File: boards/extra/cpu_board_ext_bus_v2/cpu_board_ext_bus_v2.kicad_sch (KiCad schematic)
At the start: 24 parts, among them J1 Exp. Conn. A, J2 Exp. Conn. B, J3 Power, J4 Exp. Conn. C

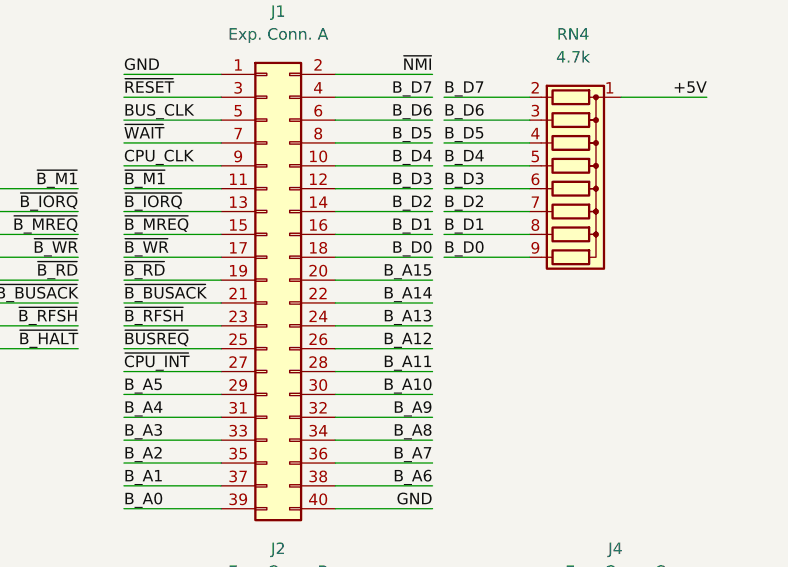
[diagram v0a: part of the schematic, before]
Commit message: Removed CPU connection A14 and A15 from Expansion Bus Connector B.
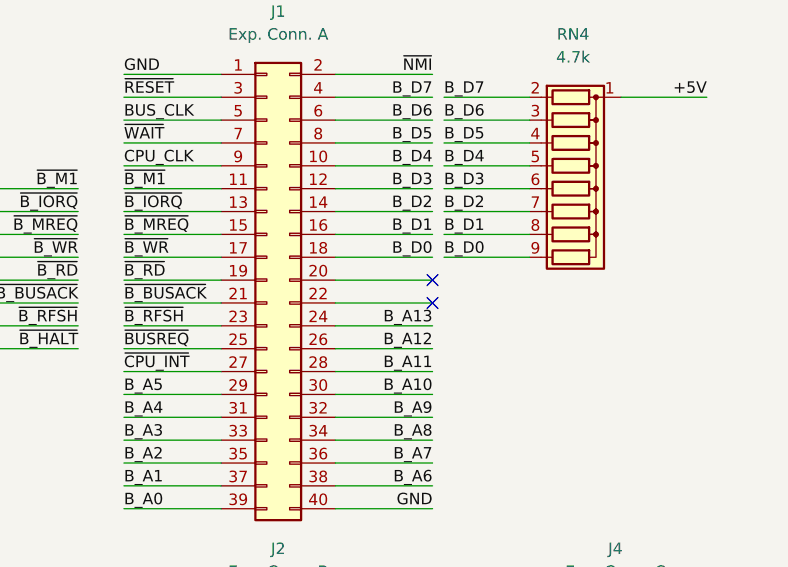
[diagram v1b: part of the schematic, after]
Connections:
- net B_A14: no longer J1.22 (Pin_22)
- net B_A15: no longer J1.20 (Pin_20)
- no-connect marks 27 -> 29
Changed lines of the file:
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@@
   (title_block
     (title "SZC-1 board with Expansion Bus C V2")
-    (date "2024-01-23")
+    (date "2024-03-15")
     (rev "2.0")
   )
@@
   (no_connect (at 356.235 110.49))
   (no_connect (at 356.235 107.95))
+  (no_connect (at 356.235 64.135))
   (no_connect (at 325.12 153.67))
   (no_connect (at 356.235 113.03))
@@
   (no_connect (at 353.06 153.67))
   (no_connect (at 356.235 138.43))
+  (no_connect (at 356.235 66.675))
   (no_connect (at 356.235 120.65))
   (no_connect (at 356.235 130.81))
@@
     (effects (font (size 1.27 1.27)) (justify right bottom))
   )
-  (label "B_A14" (at 356.235 66.675 180) (fields_autoplaced)
-    (effects (font (size 1.27 1.27)) (justify right bottom))
-  )
   (label "USER12" (at 356.235 107.95 180) (fields_autoplaced)
     (effects (font (size 1.27 1.27)) (justify right bottom))
@@
     (effects (font (size 1.27 1.27)) (justify left bottom))
   )
-  (label "B_A15" (at 356.235 64.135 180) (fields_autoplaced)
-    (effects (font (size 1.27 1.27)) (justify right bottom))
-  )
   (label "GND" (at 325.12 161.29 0) (fields_autoplaced)

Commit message: Preparation for ordering with PCBWay.
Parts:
- C1, C2: MPN (none) -> FG28X7R1H104KNT06; Manufacturer (none) -> TDK; Package (none) -> Plugin,P=5mm
- CP1: MPN (none) -> ECA1HM100I; Manufacturer (none) -> PANASONIC; Package (none) -> Plugin,D5xL11mm
- CP2: MPN (none) -> KS104M050C07RR0VH2FP0; Manufacturer (none) -> CX(Dongguan Chengxing Elec); Package (none) -> Plugin,D4xL7mm
- D1: MPN (none) -> HLMP-1700; Manufacturer (none) -> Broadcom/AVAGO; Package (none) -> LED_D3.0mm
- J1: MPN (none) -> X9555WR-2x20-6TV01; Manufacturer (none) -> XKB Connectivity; Package (none) -> Push-Pull,P=2.54mm
- J2: MPN (none) -> X9555WR-2x17-6TV01; Manufacturer (none) -> XKB Connectivity; Package (none) -> Push-Pull,P=2.54mm
- J3: MPN (none) -> X9555WR-2x10-6TV01; Manufacturer (none) -> XKB Connectivity; Package (none) -> Push-Pull,P=2.54mm
- J4: MPN (none) -> 75867-132LF; Manufacturer (none) -> Amphenol ICC; Package (none) -> Plugin
- R3: MPN (none) -> MFR2WSFTE73-1K; Manufacturer (none) -> YAGEO; Package (none) -> Plugin
- RN2, RN3, RN4: MPN (none) -> A09-472JP; Manufacturer (none) -> FH (Guangdong Fenghua Advanced Tech); Package (none) -> SIP-9-2.54mm

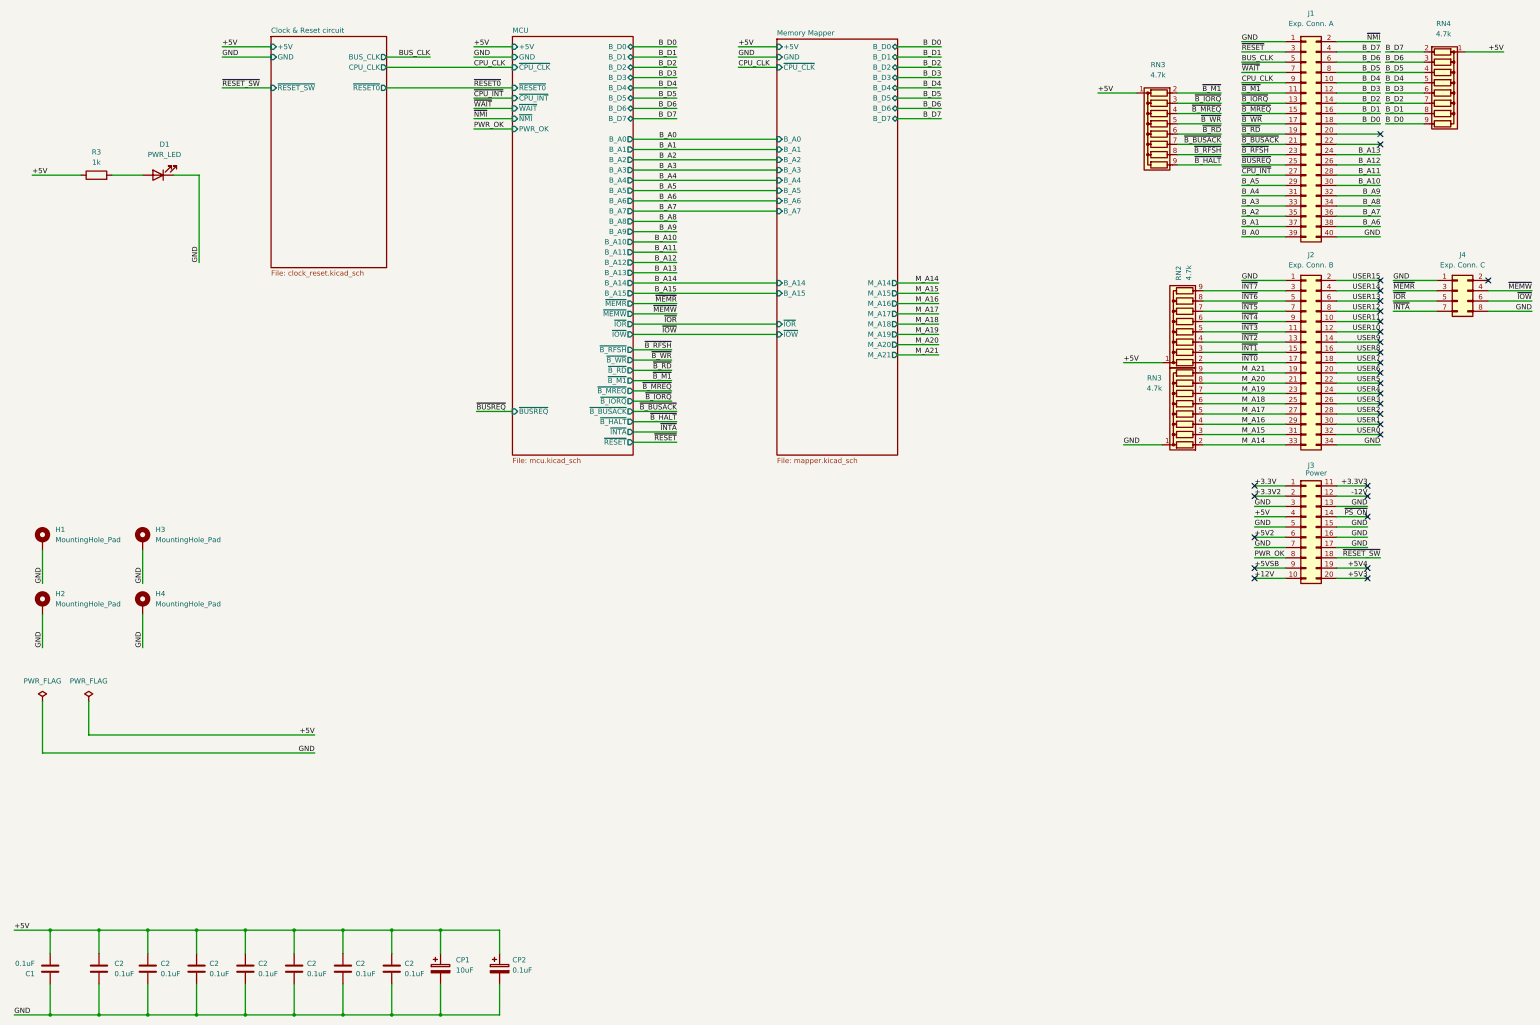
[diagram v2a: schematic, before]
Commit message: Upgraded board to KiCad 8 and imported design rules from the PCBWay website.
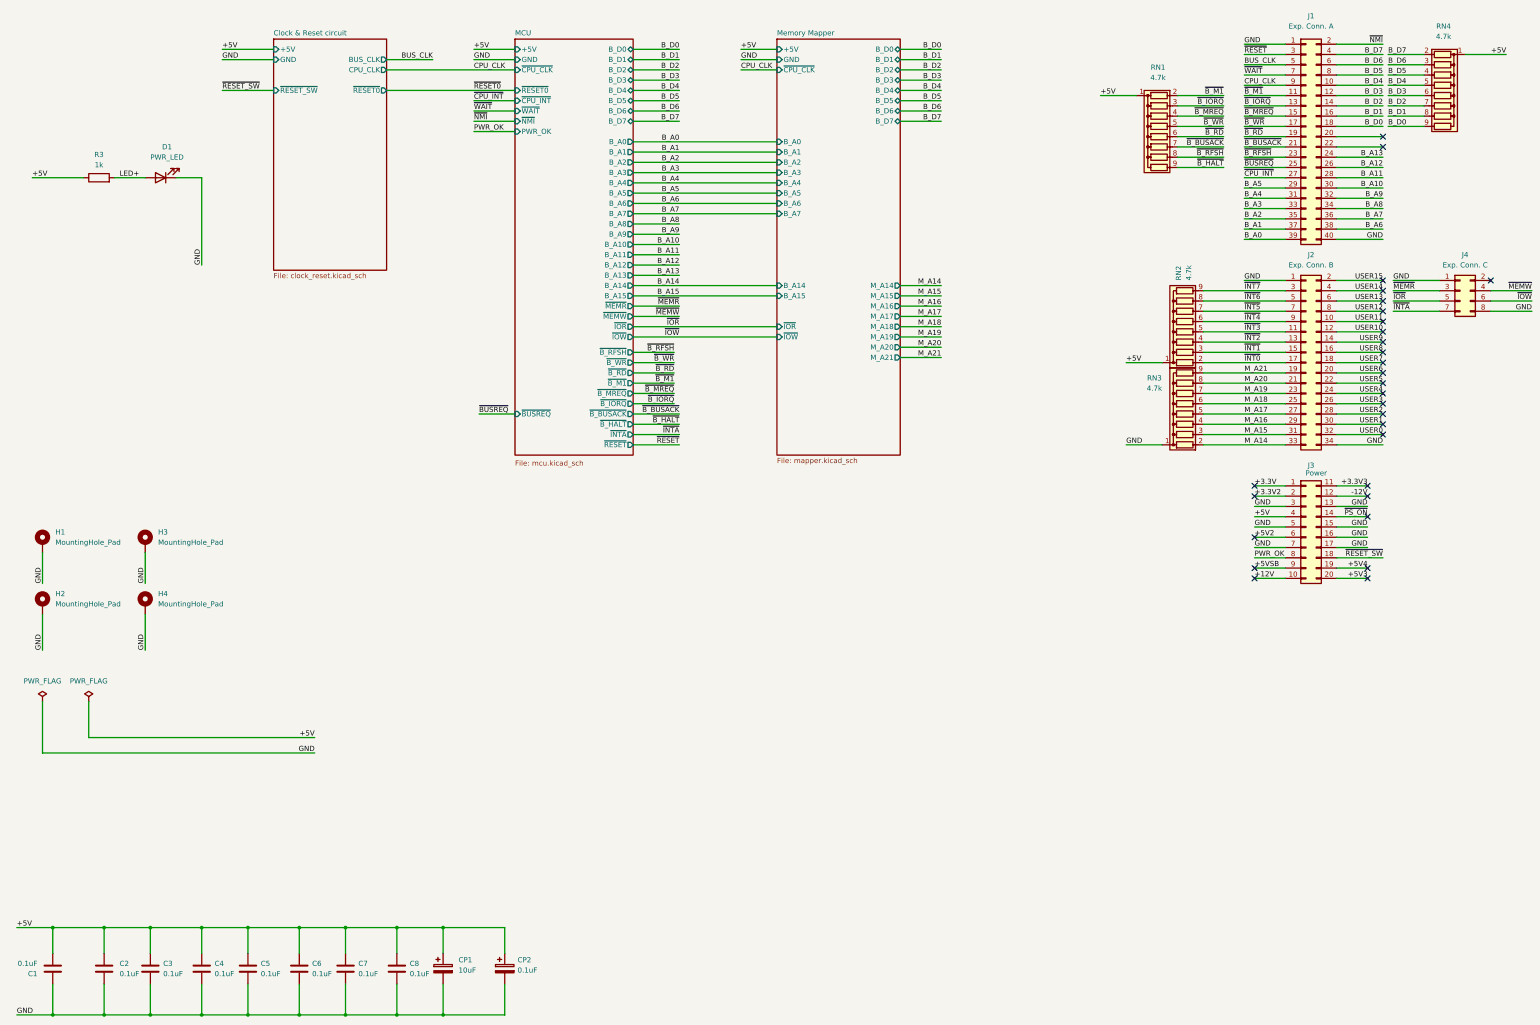
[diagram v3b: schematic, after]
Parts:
- removed C2 (x7): 0.1uF, Capacitor_THT:C_Disc_D5.0mm_W2.5mm_P2.50mm, symbol Device:C
- added C2, C3, C4, C5, C6, C7, C8: 0.1uF, Capacitor_THT:C_Disc_D5.0mm_W2.5mm_P2.50mm, symbol Device:C
- renumbered RN3 to RN1
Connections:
- net +5V: now also C2.1, C3.1, C4.1, C5.1, C6.1, C7.1, C8.1
- net GND: now also C2.2, C3.2, C4.2, C5.2, C6.2, C7.2, C8.2
- net LED+: now reaches D1.2 (A), R3.2
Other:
- moved on the sheet: D1, H1, H3, H4, J1, J4, R3, RN1, RN4
